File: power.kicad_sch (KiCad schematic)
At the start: 30 parts, among them J6 Screw_Terminal_01x02, SW1 SW_DIP_x01, SW2 SW_DIP_x01, SW3 SW_SPDT, U18 LM2940S-5.0/NOPB

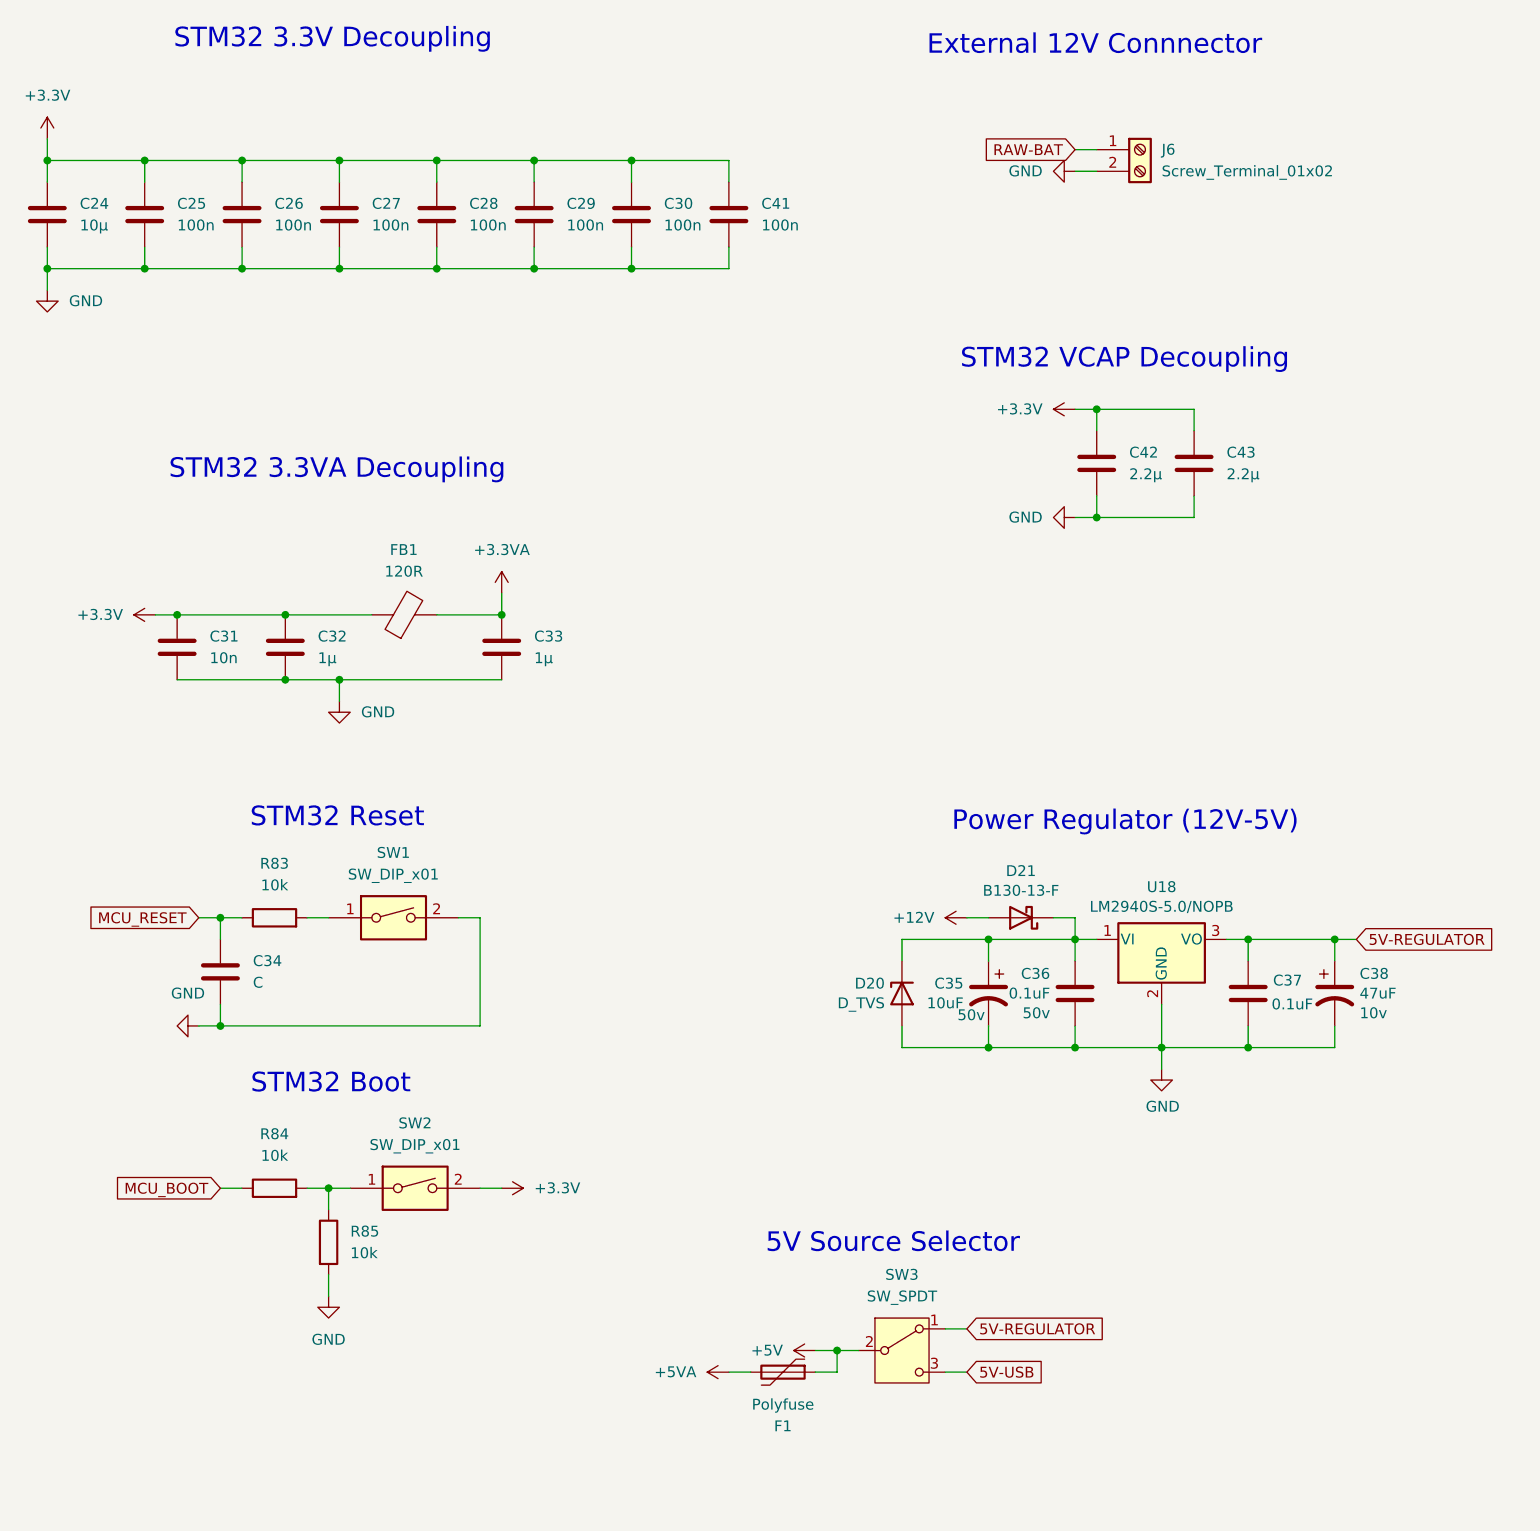
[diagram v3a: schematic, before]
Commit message: Update from Speeduino Discord suggestions (thanks to Detonator)
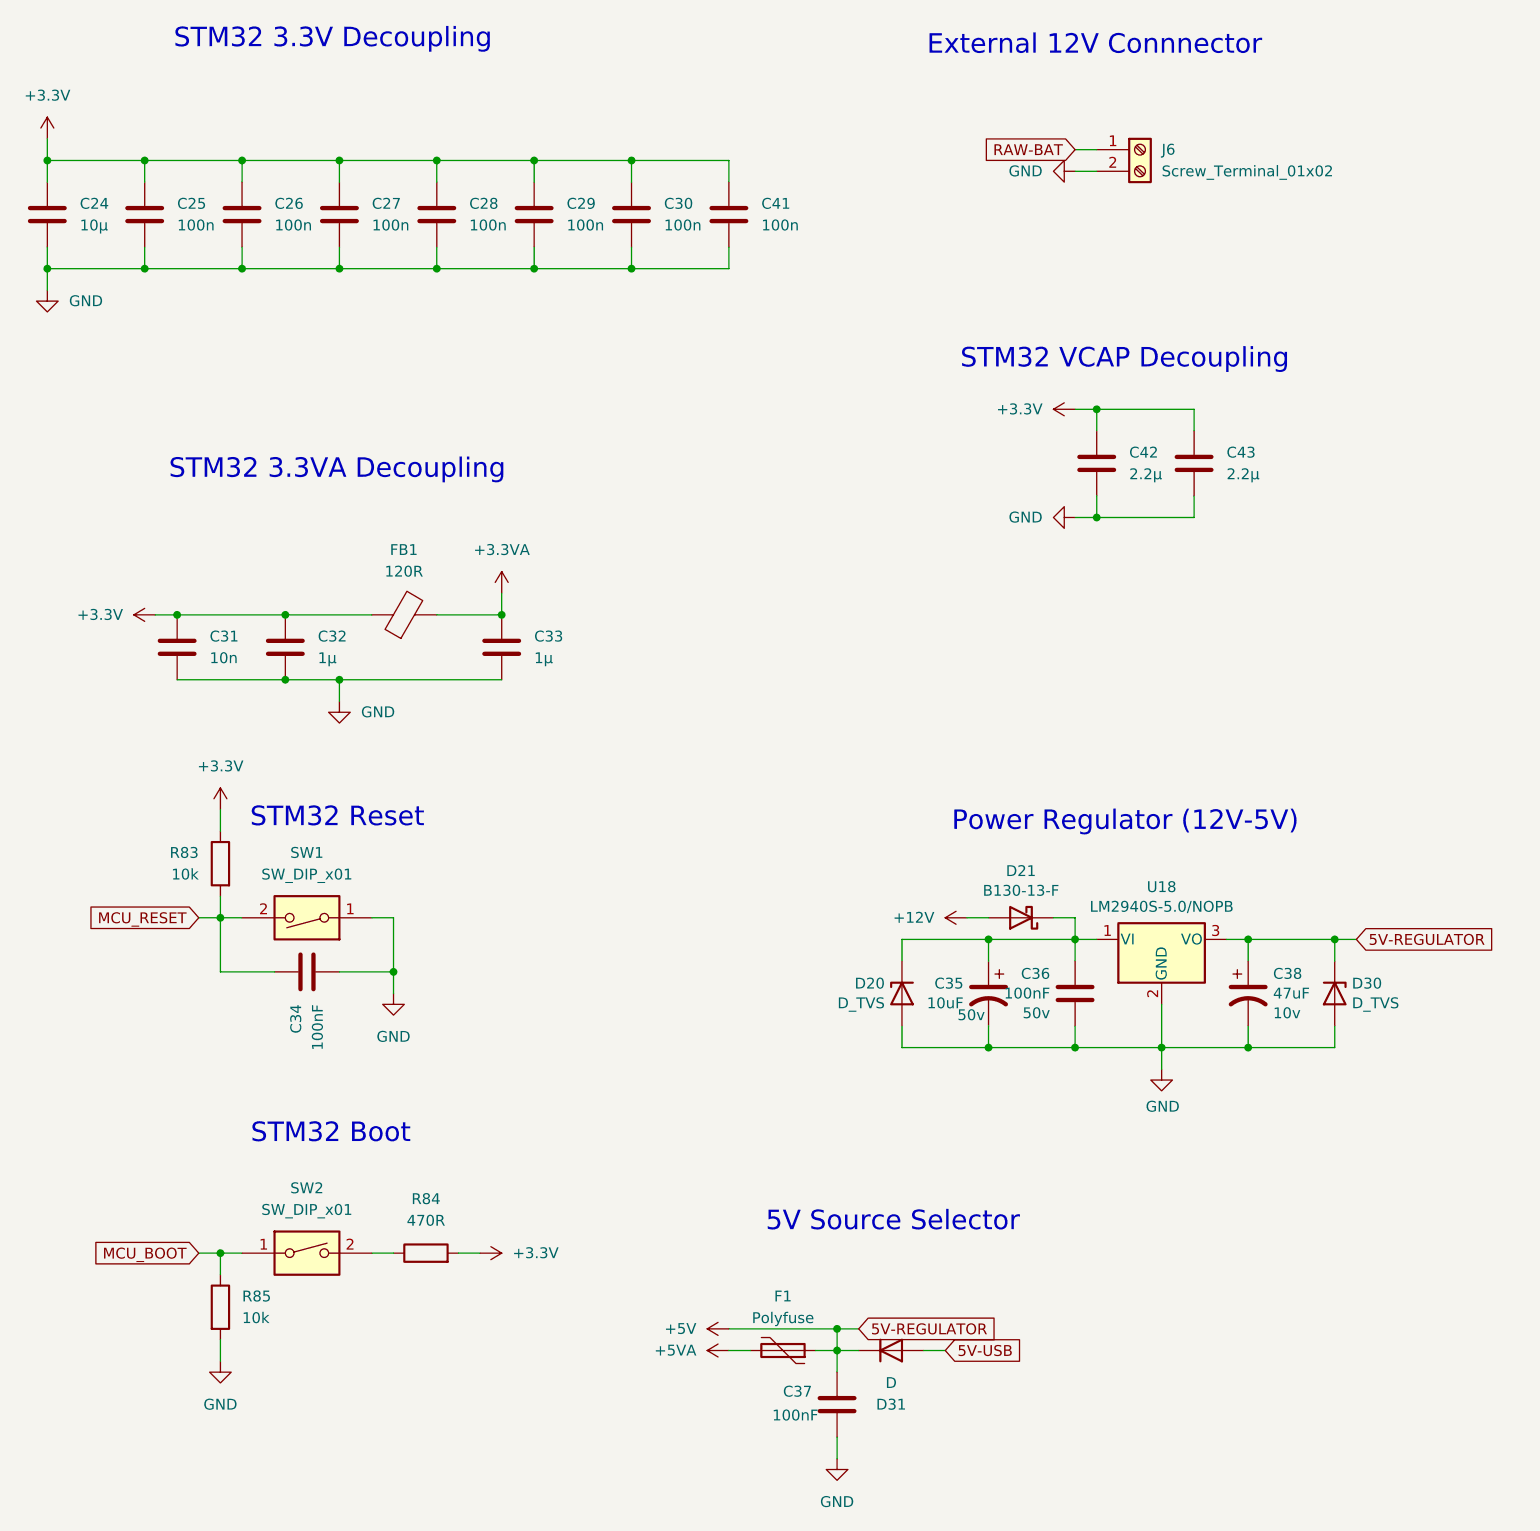
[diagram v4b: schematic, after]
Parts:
- removed SW3: SW_SPDT, Button_Switch_SMD:SW_SPDT_CK_JS102011SAQN, symbol Switch:SW_SPDT
- added D30: D_TVS, Diode_SMD:D_SMB, symbol Device:D_Zener
- added D31: D, symbol Device:D
- C34: value C -> 100nF
- C36, C37: value 0.1uF -> 100nF
- R84: value 10k -> 470R
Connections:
- net 5V-REGULATOR is gone; now on net +5V: C37.1, C38.1, U18.3 (VO)
- net +3.3V: now also R83.1, R84.2; no longer SW2.2
- net +5V: now also D30.1 (K), D31.1 (K)
- net 5V-USB: now also D31.2 (A)
- net GND: now also SW1.1, D30.2 (A); no longer SW1.2
- net MCU_BOOT: now also R85.1, SW2.1; no longer R84.1
- net MCU_RESET: now also R83.2, SW1.2; no longer R83.1
- new net: R84.1, SW2.2
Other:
- moved on the sheet: C34, C37, C38, F1, R83, R84, R85, SW1, SW2

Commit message: Fully connect all components
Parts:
- removed D31: D, symbol Device:D
- added D31: D_Schottky, Diode_SMD:D_SOD-323, symbol Device:D_Schottky
- added NT1: NetTie_2, NetTie:NetTie-2_SMD_Pad0.5mm, symbol Device:NetTie_2
- C35: value 10uF -> 470nF
- C36: Voltage 50v -> 10v
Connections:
- net RAW-BAT is gone; now on net VBAT: J6.1 (Pin_1)
- net +5V: now also D31.1 (K), NT1.1; no longer C38.1, D30.1 (K), U18.3 (VO)
- net 5V-USB: now also D31.2 (A)
- net at C35.1, D20.1 (K), D21.1 (K)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: no longer C36.1
- net +12V renamed VBAT
- new net 5V-REGULATOR: C36.1, C38.1, D30.1 (K), NT1.2, U18.3 (VO)
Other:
- note added: "5V Source Protection"
- note removed: "5V Source Selector"
- moved on the sheet: C35, C36, C37, C38, D20, D21, D30, F1, U18

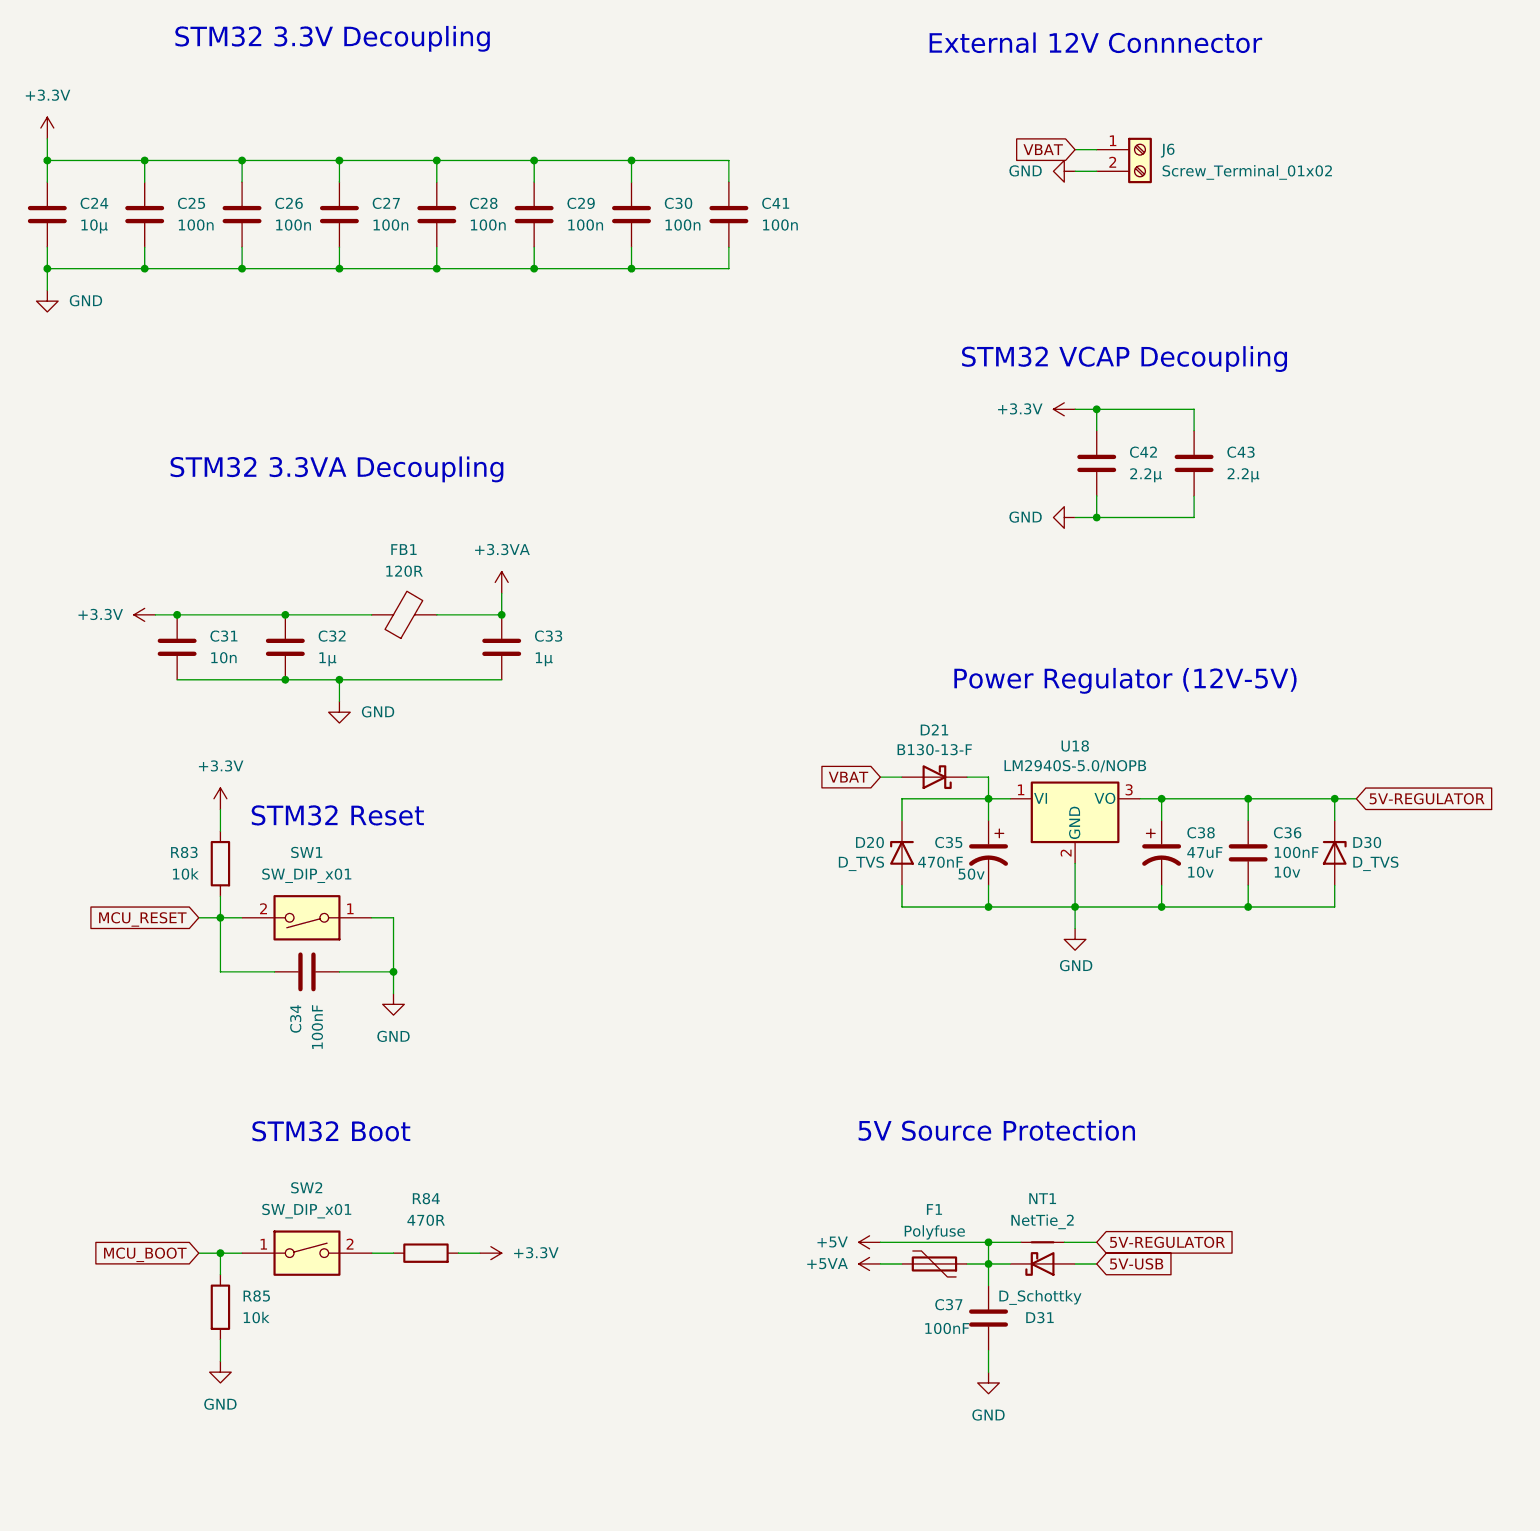
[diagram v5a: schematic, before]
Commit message: Updated reference layout
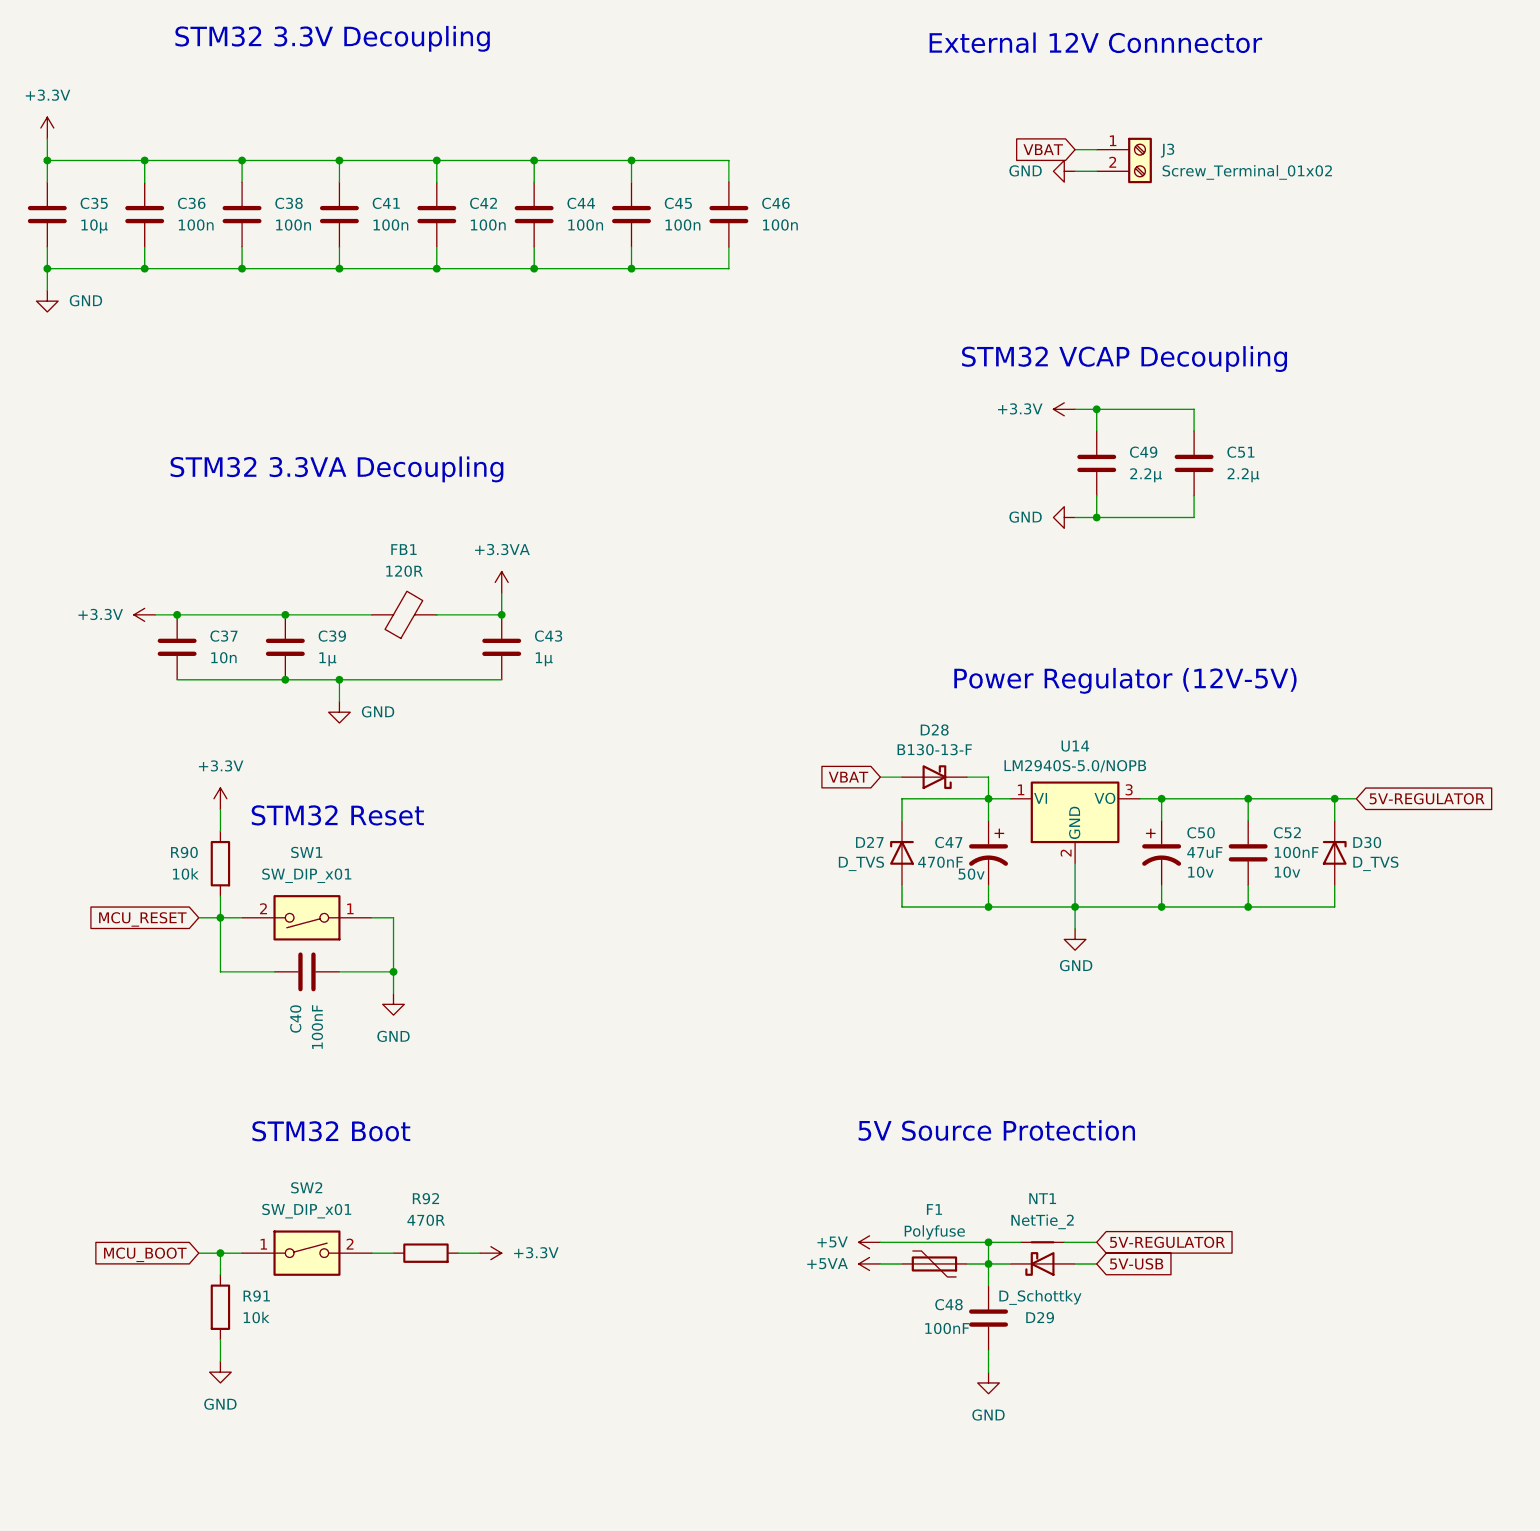
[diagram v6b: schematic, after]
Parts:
- J3: renamed from J6; footprint TerminalBlock:TerminalBlock_bornier-2_P5.08mm -> TerminalBlock_MetzConnect:TerminalBlock_MetzConnect_Type059_RT06302HBWC_1x02_P3.50mm_Horizontal
- renumbered C24 to C35, C25 to C36, C31 to C37, C26 to C38, C32 to C39, C34 to C40, C27 to C41, C28 to C42, C33 to C43, C29 to C44, C30 to C45, C41 to C46, C35 to C47, C37 to C48, C42 to C49, C38 to C50, C43 to C51, C36 to C52, D20 to D27, D21 to D28, D31 to D29, R83 to R90, R85 to R91, R84 to R92, U18 to U14
